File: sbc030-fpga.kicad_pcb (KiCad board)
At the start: 4 copper layers, 152.4 x 114.3 mm, 81 parts, among them J1 C96, J2 JTAG, J3 USB_B_Micro, U1 LFE5U-12F-8BG256C, U10 74LVC245, U11 74LVC245, U12 TXS0104E, U13 TLV62569DBVR, U14 TLV62569DBVR, U15 TLV62569DBVR, U16 FT230XS, U17 IS42S16400J-xT, U2 W25Q128JVSIQ, U3 74LVC245, U4 74LVC245, U5 74LVC245, U6 74LVC245, U7 74LVC245, U8 74LVC245, U9 74LVC245

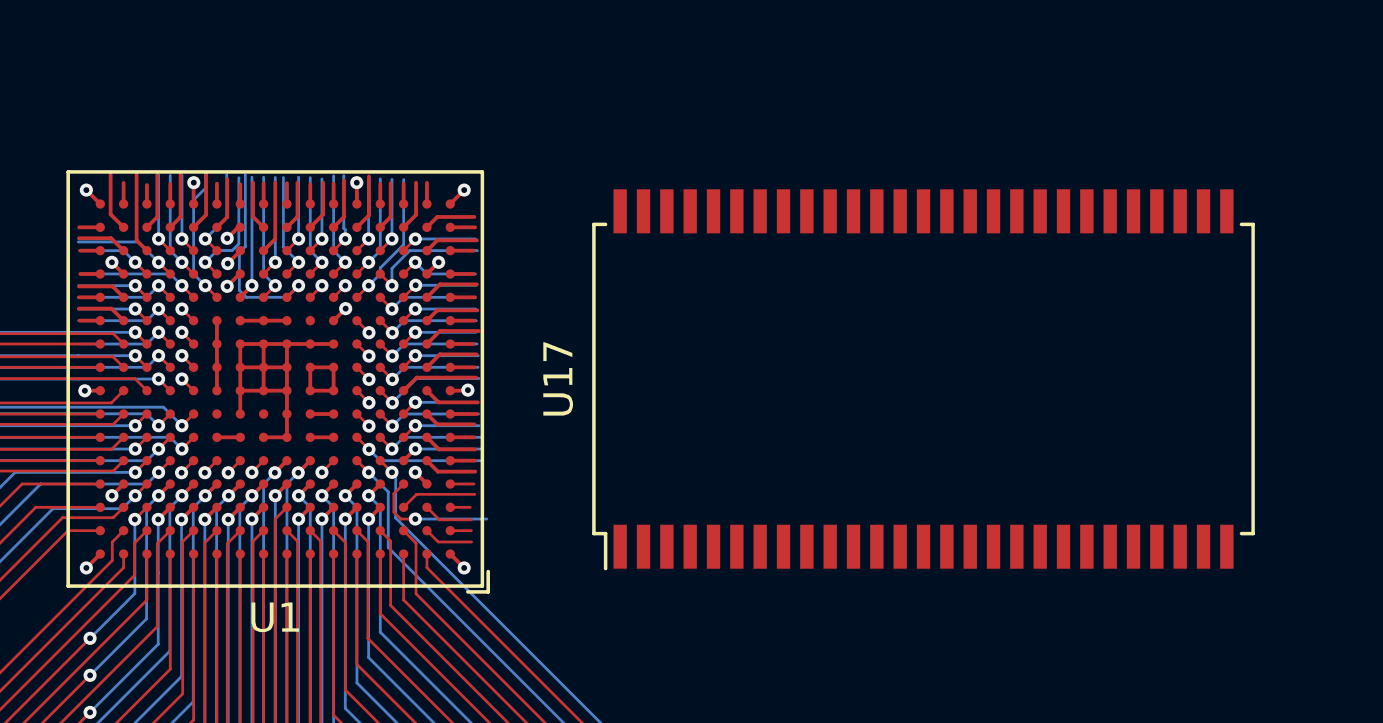
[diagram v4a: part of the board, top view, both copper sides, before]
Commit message: add sdram connections
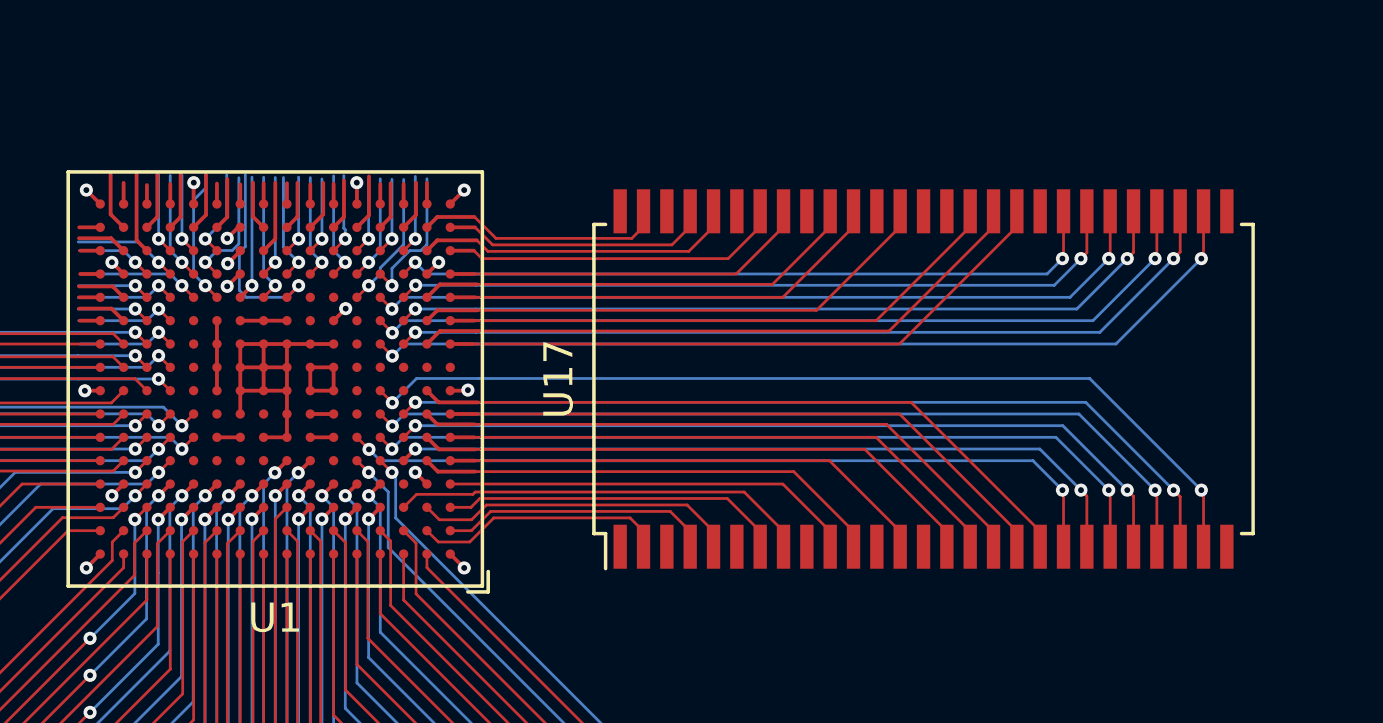
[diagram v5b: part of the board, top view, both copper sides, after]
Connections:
- U1 pad B1: Net-(U1-PadB1) -> SDRAM_DQ1
- U1 pad B2: Net-(U1-PadB2) -> SDRAM_DQ0
- U1 pad C1: Net-(U1-PadC1) -> SDRAM_DQ3
- U1 pad C2: Net-(U1-PadC2) -> SDRAM_DQ2
- U1 pad C3: Net-(U1-PadC3) -> SDRAM_DQ4
- U1 pad D1: Net-(U1-PadD1) -> SDRAM_DQ5
- U1 pad E1: Net-(U1-PadE1) -> SDRAM_DQ7
- U1 pad E2: Net-(U1-PadE2) -> SDRAM_DQ6
- U1 pad E3: Net-(U1-PadE3) -> SDRAM_BA1
- U1 pad F1: Net-(U1-PadF1) -> SDRAM_WE
- U1 pad F2: Net-(U1-PadF2) -> SDRAM_LDQM
- U1 pad F3: Net-(U1-PadF3) -> SDRAM_A0
- U1 pad F4: Net-(U1-PadF4) -> SDRAM_A10
- U1 pad F5: Net-(U1-PadF5) -> SDRAM_BA0
- U1 pad G1: Net-(U1-PadG1) -> SDRAM_RAS
- U1 pad G2: Net-(U1-PadG2) -> SDRAM_CAS
- U1 pad G3: Net-(U1-PadG3) -> SDRAM_A2
- U1 pad G4: Net-(U1-PadG4) -> SDRAM_A1
- U1 pad H2: Net-(U1-PadH2) -> SDRAM_CS
- U1 pad H4: Net-(U1-PadH4) -> SDRAM_A3
- U1 pad K1: Net-(U1-PadK1) -> SDRAM_CKE
- U1 pad K2: Net-(U1-PadK2) -> SDRAM_CLK
- U1 pad K3: Net-(U1-PadK3) -> SDRAM_A5
- U1 pad K4: Net-(U1-PadK4) -> SDRAM_A4
- U1 pad L1: Net-(U1-PadL1) -> SDRAM_UDQM
- U1 pad L2: Net-(U1-PadL2) -> SDRAM_DQ8
- U1 pad L3: Net-(U1-PadL3) -> SDRAM_A7
- U1 pad L4: Net-(U1-PadL4) -> SDRAM_A6
- U1 pad M1: Net-(U1-PadM1) -> SDRAM_DQ9
- U1 pad M2: Net-(U1-PadM2) -> SDRAM_DQ10
- U1 pad M3: Net-(U1-PadM3) -> SDRAM_A9
- U1 pad M4: Net-(U1-PadM4) -> SDRAM_A8
- U1 pad N1: Net-(U1-PadN1) -> SDRAM_DQ11
- U1 pad N3: Net-(U1-PadN3) -> SDRAM_A11
- U1 pad P1: Net-(U1-PadP1) -> SDRAM_DQ12
- U1 pad P2: Net-(U1-PadP2) -> SDRAM_DQ13
- U1 pad R1: Net-(U1-PadR1) -> SDRAM_DQ14
- U1 pad R2: Net-(U1-PadR2) -> SDRAM_DQ15
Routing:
- net SDRAM_A3: track 0.00 -> 32.2 mm, vias 0 -> 2
- net SDRAM_A4: track 0.00 -> 31.4 mm, vias 0 -> 2
- net SDRAM_A1: track 0.00 -> 30.0 mm, vias 0 -> 2
- net SDRAM_A2: track 0.00 -> 29.8 mm, vias 0 -> 2
- net SDRAM_A6: track 0.00 -> 29.4 mm, vias 0 -> 2
- net SDRAM_A5: track 0.00 -> 29.3 mm, vias 0 -> 2
- net SDRAM_A10: track 0.00 -> 28.0 mm, vias 0 -> 2
- net SDRAM_A0: track 0.00 -> 27.9 mm, vias 0 -> 2
- net SDRAM_A8: track 0.00 -> 27.5 mm, vias 0 -> 2
- net SDRAM_A7: track 0.00 -> 27.4 mm, vias 0 -> 2
- net SDRAM_BA0: track 0.00 -> 26.9 mm, vias 0 -> 2
- net SDRAM_BA1: track 0.00 -> 26.0 mm, vias 0 -> 2
- net SDRAM_A9: track 0.00 -> 25.5 mm, vias 0 -> 2
- net SDRAM_A11: track 0.00 -> 24.8 mm, vias 0 -> 2
- net SDRAM_CS: track 0.00 -> 23.5 mm
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- added copper zone on PWR, net +1V1
- added copper zone on PWR, net +3V3
- added copper zone on PWR, net +5V
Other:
- net class Default: trace_width 0.095 -> 0.13

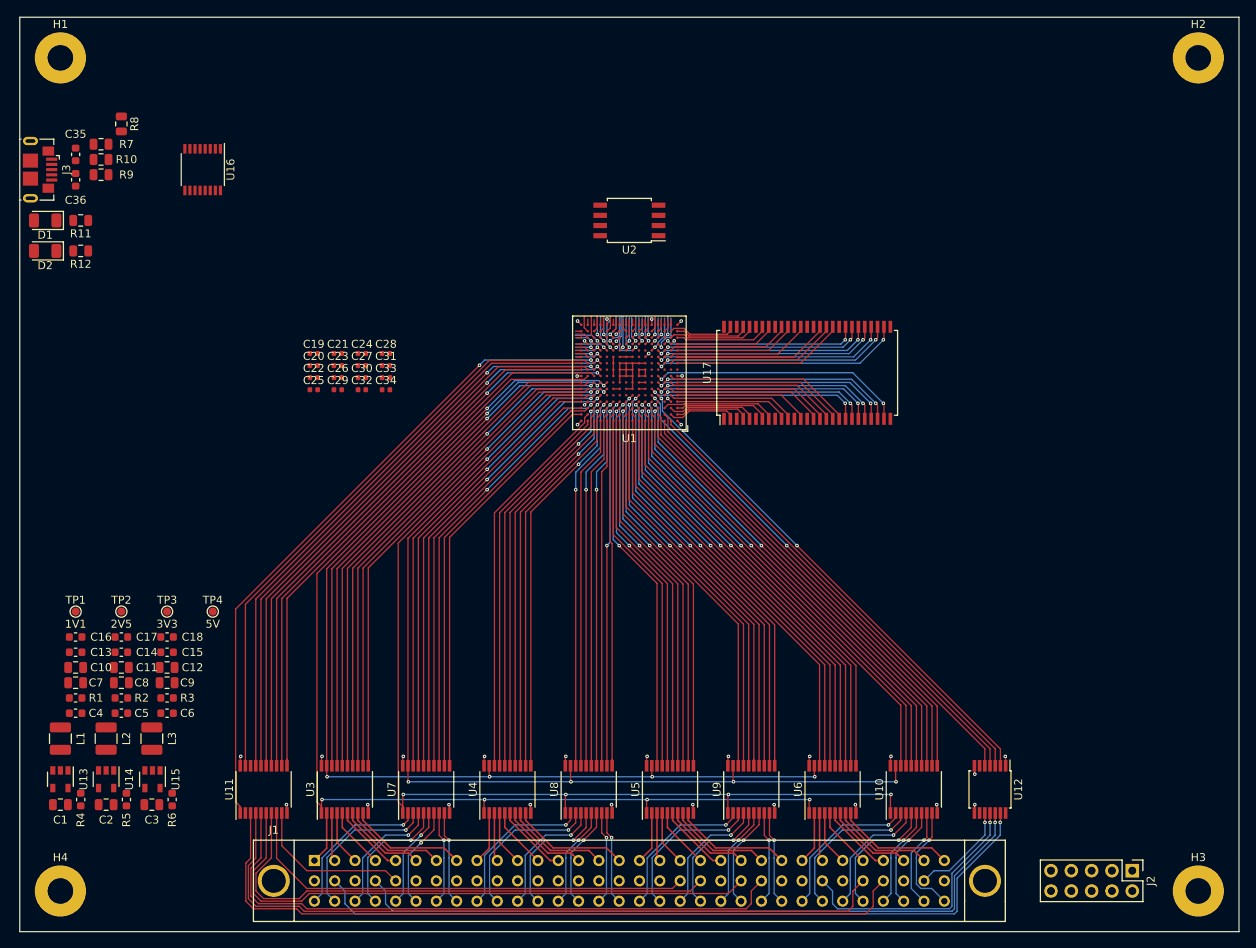
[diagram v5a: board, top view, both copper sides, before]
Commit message: add hdmi output
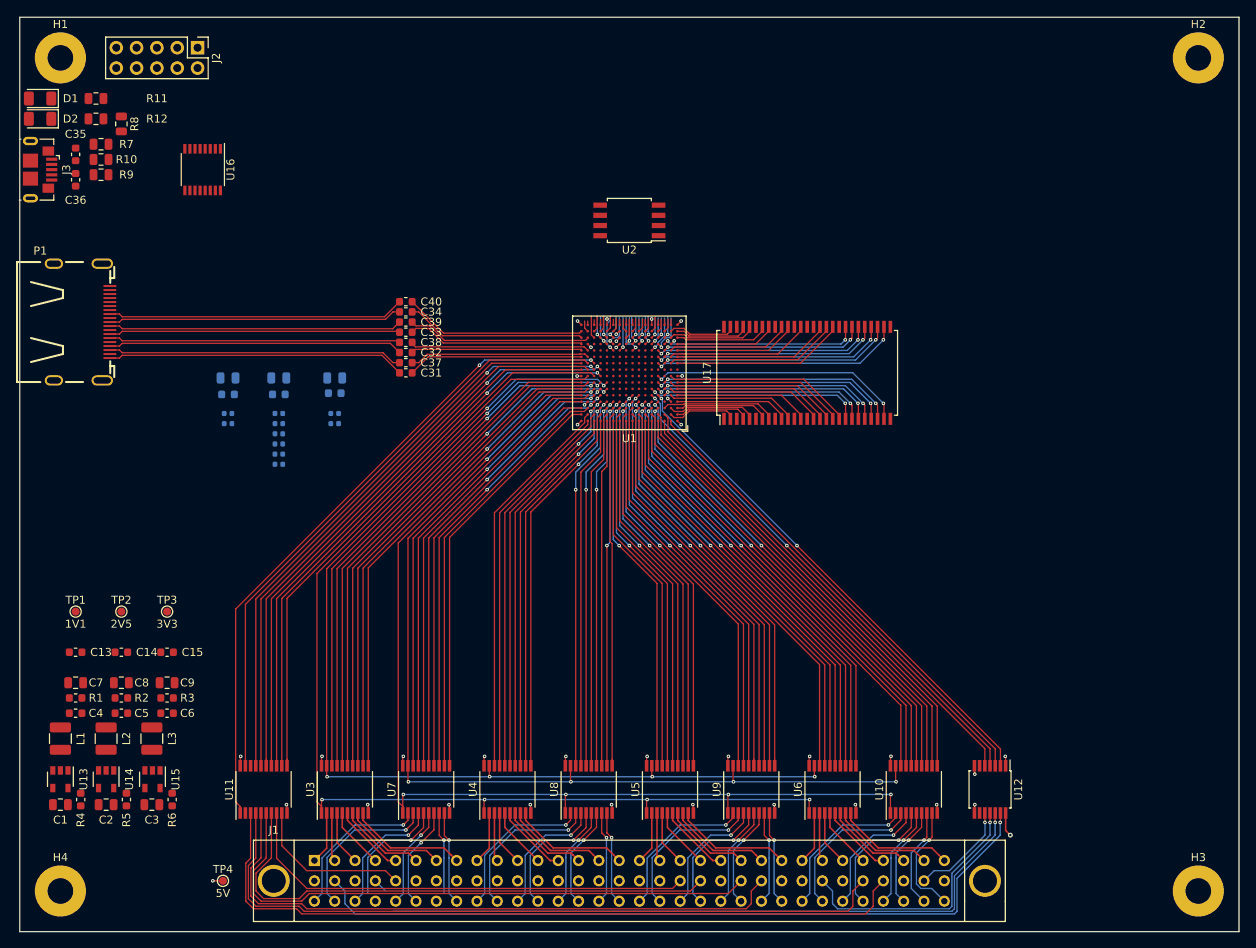
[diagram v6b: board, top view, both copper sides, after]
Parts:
- removed C29, C30: 22nF, Capacitor_SMD:C_0402_1005Metric
- added C37: 220pF, Capacitor_SMD:C_0603_1608Metric, F.Cu at (118.1, 74.9)
- added C38: 220pF, Capacitor_SMD:C_0603_1608Metric, F.Cu at (118.1, 72.4)
- added C39: 220pF, Capacitor_SMD:C_0603_1608Metric, F.Cu at (118.1, 69.8)
- added C40: 220pF, Capacitor_SMD:C_0603_1608Metric, F.Cu at (118.1, 67.3)
- added P1: HDMI-D, hdmi-d:HDMI-D, F.Cu at (75.6, 69.8)
- C10, C11, C12, C16, C17, C18, C19, C20, C21, C22, C23, C24, C25, C26, C27, C28: moved to B.Cu
- C31, C32, C33, C34: value 22nF -> 220pF; footprint Capacitor_SMD:C_0402_1005Metric -> Capacitor_SMD:C_0603_1608Metric
- moved J2 155.7 mm to (92.1, 35.6)
- moved C11 45.0 mm to (109.2, 76.8)
- moved C10 40.9 mm to (95.9, 76.8)
- moved C17 40.5 mm to (109.2, 78.7)
- moved C12 38.8 mm to (102.2, 76.8)
- moved C16 35.8 mm to (95.9, 78.9)
- moved TP4 33.7 mm to (95.2, 139.7)
- moved C18 33.4 mm to (102.2, 78.9)
- moved C28 17.5 mm to (102.2, 85.1)
- moved R12 16.6 mm to (79.4, 44.5)
- moved D2 16.5 mm to (72.4, 44.5)
- moved R11 15.4 mm to (79.4, 41.9)
- moved D1 15.3 mm to (72.4, 41.9)
- moved C19 14.5 mm to (102.2, 87.6)
- moved C20 12.9 mm to (95.9, 82.5)
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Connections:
- C31 pad 1: +3V3 -> /HDMI/D2+
- C31 pad 2: GND -> /HDMI/HDMI_D2+
- C32 pad 1: +3V3 -> /HDMI/D1+
- C32 pad 2: GND -> /HDMI/HDMI_D1+
- C33 pad 1: +3V3 -> /HDMI/D0+
- C33 pad 2: GND -> /HDMI/HDMI_D0+
- C34 pad 1: +3V3 -> /HDMI/CK+
- C34 pad 2: GND -> /HDMI/HDMI_CK+
- U1 pad L15: Net-(U1-PadL15) -> /HDMI/HDMI_D2-
- U1 pad L16: Net-(U1-PadL16) -> /HDMI/HDMI_D2+
- U1 pad M15: Net-(U1-PadM15) -> /HDMI/HDMI_D1-
- U1 pad M16: Net-(U1-PadM16) -> /HDMI/HDMI_D1+
- U1 pad N16: Net-(U1-PadN16) -> /HDMI/HDMI_D0+
- U1 pad P15: Net-(U1-PadP15) -> /HDMI/HDMI_D0-
- U1 pad P16: Net-(U1-PadP16) -> /HDMI/HDMI_CK+
- U1 pad R16: Net-(U1-PadR16) -> /HDMI/HDMI_CK-
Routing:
- net /HDMI/D2+: track 0.00 -> 37.3 mm
- net /HDMI/CK-: track 0.00 -> 37.1 mm
- net /HDMI/D2-: track 0.00 -> 36.9 mm
- net /HDMI/D1+: track 0.00 -> 36.8 mm
- net /HDMI/CK+: track 0.00 -> 36.7 mm
- net /HDMI/D0-: track 0.00 -> 36.7 mm
- net /HDMI/D1-: track 0.00 -> 36.4 mm
- net /HDMI/D0+: track 0.00 -> 36.4 mm
- net /HDMI/HDMI_D0-: track 0.00 -> 23.1 mm
- net /HDMI/HDMI_CK-: track 0.00 -> 22.9 mm
- net /HDMI/HDMI_D2-: track 0.00 -> 22.5 mm
- net /HDMI/HDMI_CK+: track 0.00 -> 22.5 mm
- net /HDMI/HDMI_D1-: track 0.00 -> 22.5 mm
- net /HDMI/HDMI_D0+: track 0.00 -> 22.2 mm
- net /HDMI/HDMI_D2+: track 0.00 -> 22.0 mm
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
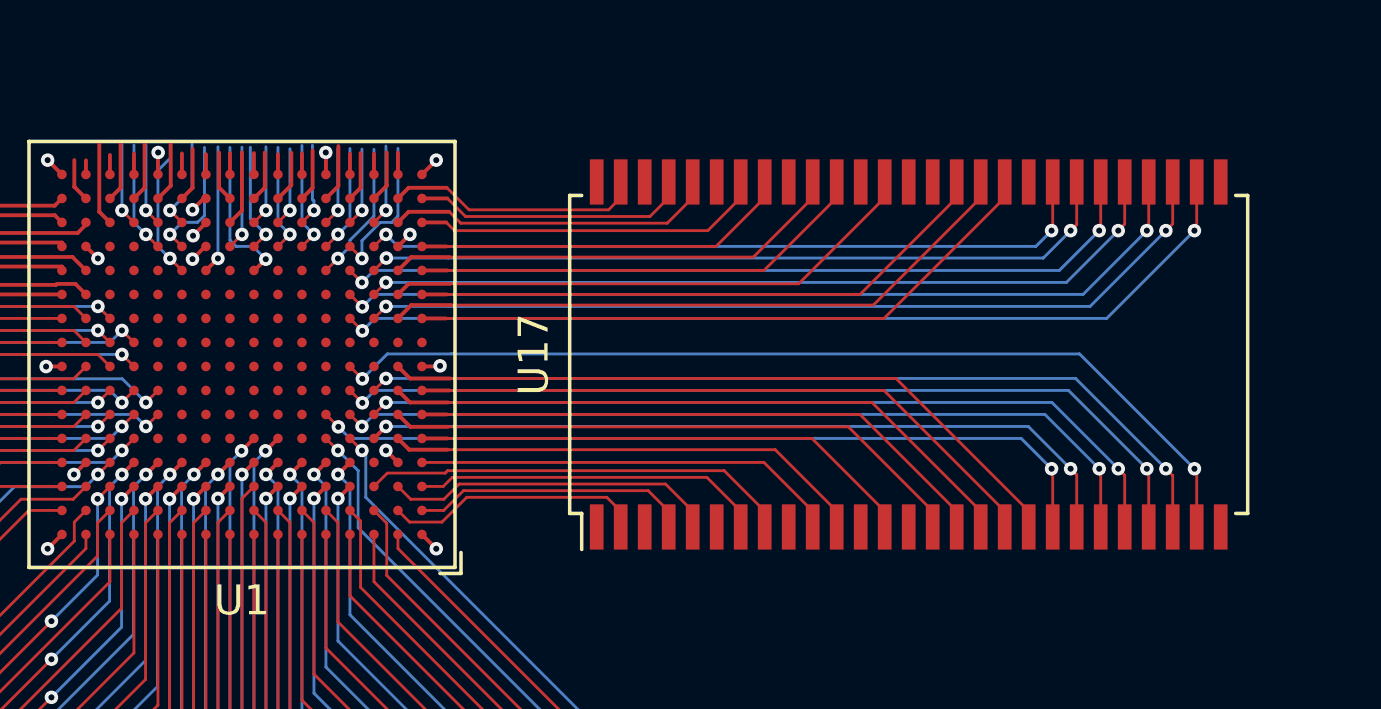
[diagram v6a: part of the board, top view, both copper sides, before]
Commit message: small pin change in sdram
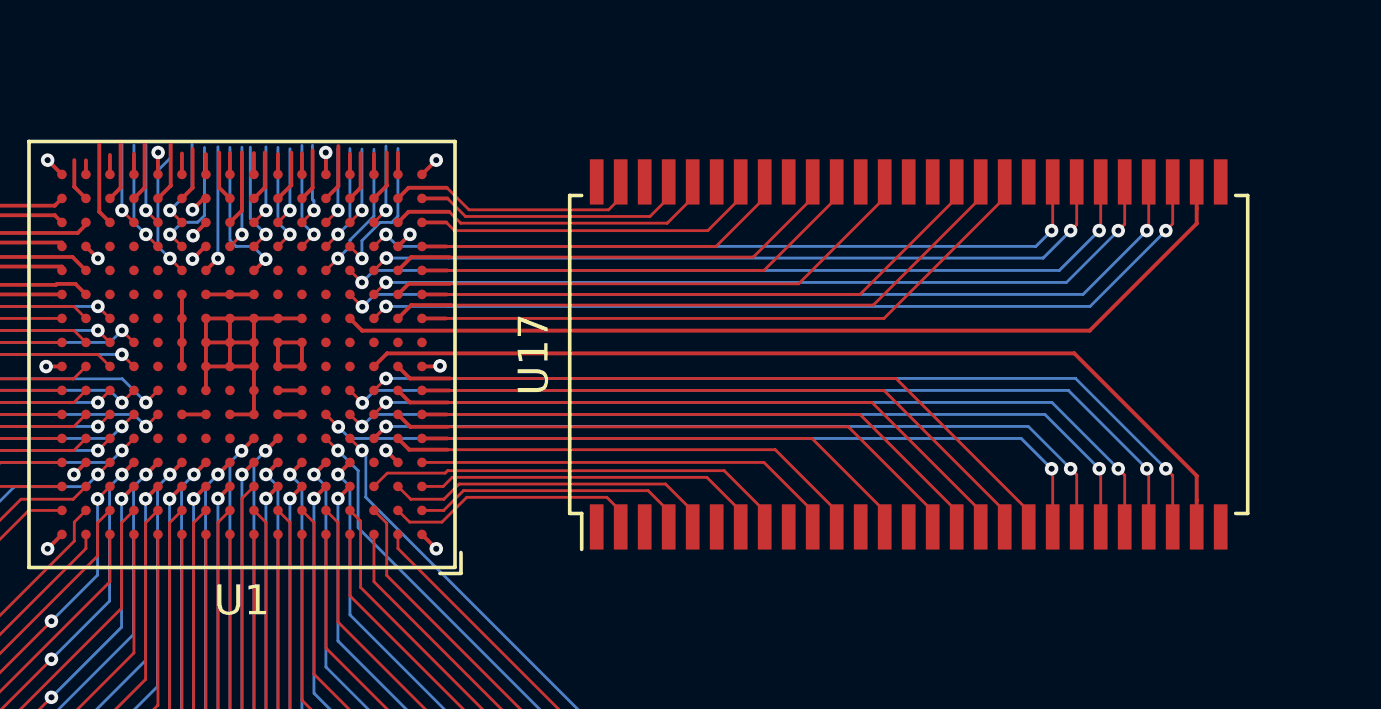
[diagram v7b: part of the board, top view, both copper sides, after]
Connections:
- U1 pad H3: Net-(U1-PadH3) -> SDRAM_A3
- U1 pad H4: SDRAM_A3 -> Net-(U1-PadH4)
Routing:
- net GND: track 19.7 -> 34.1 mm
- net +3V3: track 14.0 -> 21.2 mm
- net +1V1: track 0.10 -> 2.50 mm
- net SDRAM_A3: track 32.2 -> 31.0 mm, vias 2 -> 0
- net SDRAM_A4: track 31.4 -> 31.3 mm, vias 2 -> 0
